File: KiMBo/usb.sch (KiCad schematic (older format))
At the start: 19 parts, among them U1 OSD3358, U6 TPS2051B, U7 TPD4S012, U8 74LVC2G241, U9 TPD4S012

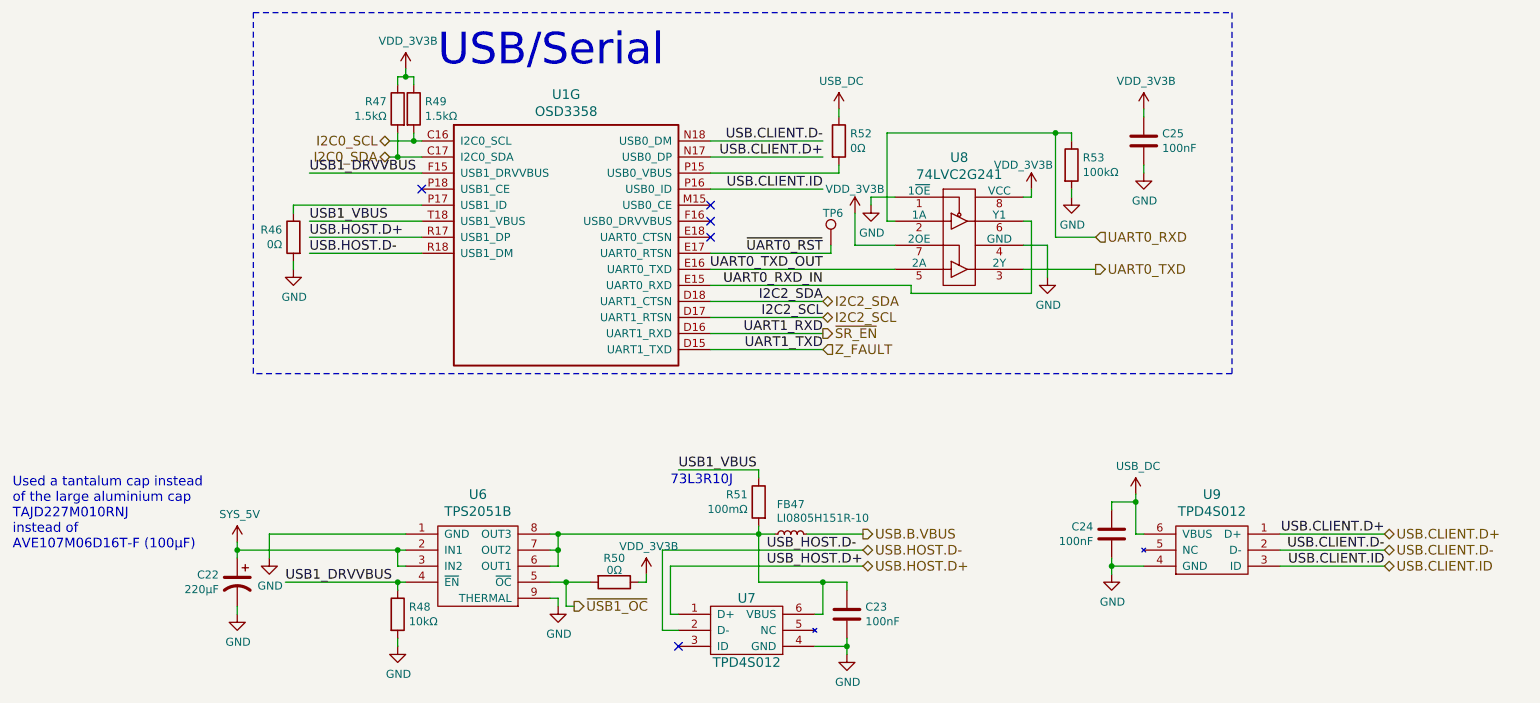
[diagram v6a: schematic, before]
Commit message: Remove the unneeded oscillator, track down which components are underneath the OSD3358 and put them on the top
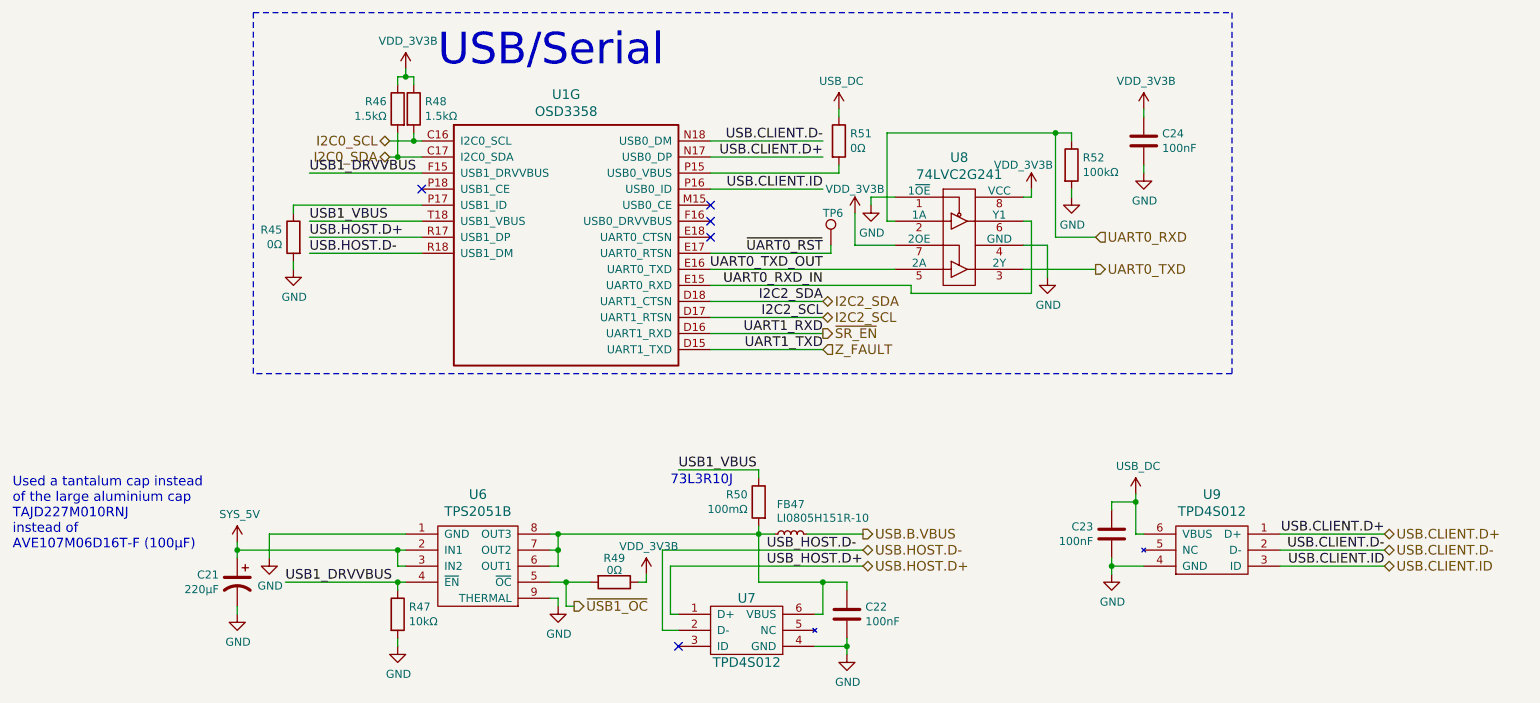
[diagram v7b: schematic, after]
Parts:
- renumbered C22 to C21, C23 to C22, C24 to C23, C25 to C24, R46 to R45, R47 to R46, R48 to R47, R49 to R48, R50 to R49, R51 to R50, R52 to R51, R53 to R52
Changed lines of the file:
@@
 $EndComp
 $Comp
-L GND #PWR099
+L GND #PWR097
 U 1 1 584F5078
 P 7550 2500
-F 0 "#PWR099" H 7550 2250 50  0001 C CNN
+F 0 "#PWR097" H 7550 2250 50  0001 C CNN
 F 1 "GND" H 7555 2327 50  0000 C CNN
 F 2 "" H 7550 2500 50  0000 C CNN
@@
 UART0_RXD_IN
 $Comp
-L R R53
+L R R52
 U 1 1 584F5085
 P 7700 1800
-F 0 "R53" H 7770 1846 50  0000 L CNN
+F 0 "R52" H 7770 1846 50  0000 L CNN
 F 1 "100kΩ" H 7770 1755 50  0000 L CNN
 F 2 "Resistors_SMD:R_0603" V 7630 1800 50  0001 C CNN
@@
 $EndComp
 $Comp
-L GND #PWR0100
+L GND #PWR098
 U 1 1 584F508C
 P 6450 2050
-F 0 "#PWR0100" H 6450 1800 50  0001 C CNN
+F 0 "#PWR098" H 6450 1800 50  0001 C CNN
 F 1 "GND" H 6455 1877 50  0000 C CNN
 F 2 "" H 6450 2050 50  0000 C CNN
@@
 UART0_TXD_OUT
 $Comp
-L GND #PWR0101
+L GND #PWR099
 U 1 1 584F509A
 P 7700 2000
-F 0 "#PWR0101" H 7700 1750 50  0001 C CNN
+F 0 "#PWR099" H 7700 1750 50  0001 C CNN
 F 1 "GND" H 7705 1827 50  0000 C CNN
 F 2 "" H 7700 2000 50  0000 C CNN
@@
 $EndComp
 $Comp
-L C C25
+L C C24
 U 1 1 584F50A3
 P 8150 1650
-F 0 "C25" H 8265 1696 50  0000 L CNN
+F 0 "C24" H 8265 1696 50  0000 L CNN
 F 1 "100nF" H 8265 1605 50  0000 L CNN
 F 2 "Capacitors_SMD:C_0603" H 8150 1650 50  0001 C CNN
@@
 $EndComp
 $Comp
-L GND #PWR0102
+L GND #PWR0100
 U 1 1 584F50AA
 P 8150 1850
-F 0 "#PWR0102" H 8150 1600 50  0001 C CNN
+F 0 "#PWR0100" H 8150 1600 50  0001 C CNN
 F 1 "GND" H 8155 1677 50  0000 C CNN
 F 2 "" H 8150 1850 50  0000 C CNN
@@
 NoConn ~ 5450 2150
 $Comp
-L R R52
+L R R51
 U 1 1 584F50C1
 P 6250 1650
-F 0 "R52" H 6320 1696 50  0000 L CNN
+F 0 "R51" H 6320 1696 50  0000 L CNN
 F 1 "0Ω" H 6320 1605 50  0000 L CNN
 F 2 "Resistors_SMD:R_0603" V 6180 1650 50  0001 C CNN
@@
 NoConn ~ 3650 1950
 $Comp
-L R R46
+L R R45
 U 1 1 584F50D1
 P 2850 2250
-F 0 "R46" H 2920 2296 50  0000 L CNN
+F 0 "R45" H 2920 2296 50  0000 L CNN
 F 1 "0Ω" H 2920 2205 50  0000 L CNN
 F 2 "Resistors_SMD:R_0603" V 2780 2250 50  0001 C CNN
@@
 $EndComp
 $Comp
-L GND #PWR0103
+L GND #PWR0101
 U 1 1 584F50D8
 P 2850 2450
-F 0 "#PWR0103" H 2850 2200 50  0001 C CNN
+F 0 "#PWR0101" H 2850 2200 50  0001 C CNN
 F 1 "GND" H 2855 2277 50  0000 C CNN
 F 2 "" H 2850 2450 50  0000 C CNN
@@
 USB1_DRVVBUS
 $Comp
-L R R47
+L R R46
 U 1 1 584F50E0
 P 3500 1450
-F 0 "R47" H 3569 1496 50  0000 L CNN
+F 0 "R46" H 3569 1496 50  0000 L CNN
 F 1 "1.5kΩ" H 3569 1405 50  0000 L CNN
 F 2 "Resistors_SMD:R_0603" V 3430 1450 50  0001 C CNN
@@
 $EndComp
 $Comp
-L R R49
+L R R48
 U 1 1 584F50E7
 P 3600 1450
-F 0 "R49" H 3670 1496 50  0000 L CNN
+F 0 "R48" H 3670 1496 50  0000 L CNN
 F 1 "1.5kΩ" H 3670 1405 50  0000 L CNN
 F 2 "Resistors_SMD:R_0603" V 3530 1450 50  0001 C CNN
@@
 $EndComp
 $Comp
-L C C23
+L C C22
 U 1 1 58524285
 P 6300 4600
-F 0 "C23" H 6415 4646 50  0000 L CNN
+F 0 "C22" H 6415 4646 50  0000 L CNN
 F 1 "100nF" H 6415 4555 50  0000 L CNN
 F 2 "Capacitors_SMD:C_0603" H 6300 4600 50  0001 C CNN
@@
 $EndComp
 $Comp
-L GND #PWR0104
+L GND #PWR0102
 U 1 1 585243B8
 P 6300 4850
-F 0 "#PWR0104" H 6300 4600 50  0001 C CNN
+F 0 "#PWR0102" H 6300 4600 50  0001 C CNN
 F 1 "GND" H 6305 4677 50  0000 C CNN
 F 2 "" H 6300 4850 50  0000 C CNN
@@
 $EndComp
 $Comp
-L GND #PWR0105
+L GND #PWR0103
 U 1 1 58528602
 P 4500 4550
-F 0 "#PWR0105" H 4500 4300 50  0001 C CNN
+F 0 "#PWR0103" H 4500 4300 50  0001 C CNN
 F 1 "GND" H 4505 4377 50  0000 C CNN
 F 2 "" H 4500 4550 50  0000 C CNN
@@
 $EndComp
 $Comp
-L R R50
+L R R49
 U 1 1 58528C30
 P 4850 4400
-F 0 "R50" V 4700 4400 50  0000 C CNN
+F 0 "R49" V 4700 4400 50  0000 C CNN
 F 1 "0Ω" V 4775 4400 50  0000 C CNN
 F 2 "Resistors_SMD:R_0603" V 4780 4400 50  0001 C CNN
@@
 $EndComp
 $Comp
-L GND #PWR0106
+L GND #PWR0104
 U 1 1 5852A6BE
 P 2500 4600
-F 0 "#PWR0106" H 2500 4350 50  0001 C CNN
+F 0 "#PWR0104" H 2500 4350 50  0001 C CNN
 F 1 "GND" H 2505 4427 50  0000 C CNN
 F 2 "" H 2500 4600 50  0000 C CNN
@@
 $EndComp
 $Comp
-L GND #PWR0107
+L GND #PWR0105
 U 1 1 5852A82F
 P 2700 4250
-F 0 "#PWR0107" H 2700 4000 50  0001 C CNN
+F 0 "#PWR0105" H 2700 4000 50  0001 C CNN
 F 1 "GND" H 2705 4077 50  0000 C CNN
 F 2 "" H 2700 4250 50  0000 C CNN
@@
 USB1_DRVVBUS
 $Comp
-L R R48
+L R R47
 U 1 1 5852B51B
 P 3500 4600
-F 0 "R48" H 3570 4646 50  0000 L CNN
+F 0 "R47" H 3570 4646 50  0000 L CNN
 F 1 "10kΩ" H 3570 4555 50  0000 L CNN
 F 2 "Resistors_SMD:R_0603" V 3430 4600 50  0001 C CNN
@@
 $EndComp
 $Comp
-L GND #PWR0108
+L GND #PWR0106
 U 1 1 5852B68C
 P 3500 4800
-F 0 "#PWR0108" H 3500 4550 50  0001 C CNN
+F 0 "#PWR0106" H 3500 4550 50  0001 C CNN
 F 1 "GND" H 3505 4627 50  0000 C CNN
 F 2 "" H 3500 4800 50  0000 C CNN
@@
 $EndComp
 $Comp
-L C C24
+L C C23
 U 1 1 5852C2E6
 P 7950 4100
-F 0 "C24" H 8065 4146 50  0000 L CNN
+F 0 "C23" H 8065 4146 50  0000 L CNN
 F 1 "100nF" H 8065 4055 50  0000 L CNN
 F 2 "Capacitors_SMD:C_0603" H 7950 4100 50  0001 C CNN
@@
 I2C2_SDA
 $Comp
-L USB_DC #PWR0109
+L USB_DC #PWR0107
 U 1 1 59F94F9A
 P 8100 3850
-F 0 "#PWR0109" H 8100 3700 50  0001 C CNN
+F 0 "#PWR0107" H 8100 3700 50  0001 C CNN
 F 1 "USB_DC" H 8115 4023 50  0000 C CNN
 F 2 "" H 8100 3850 50  0000 C CNN
@@
 $EndComp
 $Comp
-L SYS_5V #PWR0110
+L SYS_5V #PWR0108
 U 1 1 59F970D0
 P 2500 4150
-F 0 "#PWR0110" H 2500 4000 50  0001 C CNN
+F 0 "#PWR0108" H 2500 4000 50  0001 C CNN
 F 1 "SYS_5V" H 2515 4323 50  0000 C CNN
 F 2 "" H 2500 4150 50  0000 C CNN
@@
 $EndComp
 $Comp
-L VDD_3V3B #PWR0111
+L VDD_3V3B #PWR0109
 U 1 1 59FBF8B1
 P 6350 2100
-F 0 "#PWR0111" H 6350 1950 50  0001 C CNN
+F 0 "#PWR0109" H 6350 1950 50  0001 C CNN
 F 1 "VDD_3V3B" H 6350 2250 50  0000 C CNN
 F 2 "" H 6350 2100 50  0000 C CNN
@@
 $EndComp
 $Comp
-L VDD_3V3B #PWR0112
+L VDD_3V3B #PWR0110
 U 1 1 59FBF8FC
 P 7450 1950
-F 0 "#PWR0112" H 7450 1800 50  0001 C CNN
+F 0 "#PWR0110" H 7450 1800 50  0001 C CNN
 F 1 "VDD_3V3B" H 7400 2100 50  0000 C CNN
 F 2 "" H 7450 1950 50  0000 C CNN
@@
 $EndComp
 $Comp
-L VDD_3V3B #PWR0113
+L VDD_3V3B #PWR0111
 U 1 1 59FC0162
 P 8150 1450
-F 0 "#PWR0113" H 8150 1300 50  0001 C CNN
+F 0 "#PWR0111" H 8150 1300 50  0001 C CNN
 F 1 "VDD_3V3B" H 8165 1623 50  0000 C CNN
 F 2 "" H 8150 1450 50  0000 C CNN
@@
 $EndComp
 $Comp
-L USB_DC #PWR0114
+L USB_DC #PWR0112
 U 1 1 59FEDDB0
 P 6250 1450
-F 0 "#PWR0114" H 6250 1300 50  0001 C CNN
+F 0 "#PWR0112" H 6250 1300 50  0001 C CNN
 F 1 "USB_DC" H 6265 1623 50  0000 C CNN
 F 2 "" H 6250 1450 50  0000 C CNN
@@
 $EndComp
 $Comp
-L VDD_3V3B #PWR0115
+L VDD_3V3B #PWR0113
 U 1 1 5A01DA26
 P 3550 1200
-F 0 "#PWR0115" H 3550 1050 50  0001 C CNN
+F 0 "#PWR0113" H 3550 1050 50  0001 C CNN
 F 1 "VDD_3V3B" H 3565 1373 50  0000 C CNN
 F 2 "" H 3550 1200 50  0000 C CNN
@@
 Used a tantalum cap instead\nof the large aluminium cap\nTAJD227M010RNJ\ninstead of\nAVE107M06D16T-F (100μF)
 $Comp
-L VDD_3V3B #PWR0116
+L VDD_3V3B #PWR0114
 U 1 1 5AF563FC
 P 5050 4350
-F 0 "#PWR0116" H 5050 4200 50  0001 C CNN
+F 0 "#PWR0114" H 5050 4200 50  0001 C CNN
 F 1 "VDD_3V3B" H 5065 4523 50  0000 C CNN
 F 2 "" H 5050 4350 50  0000 C CNN
@@
 $EndComp
 $Comp
-L GND #PWR0117
+L GND #PWR0115
 U 1 1 5BC77EEA
 P 7950 4350
-F 0 "#PWR0117" H 7950 4100 50  0001 C CNN
+F 0 "#PWR0115" H 7950 4100 50  0001 C CNN
 F 1 "GND" H 7955 4177 50  0000 C CNN
 F 2 "" H 7950 4350 50  0000 C CNN
@@
 	6200 2350 6200 2300
 $Comp
-L R R51
+L R R50
 U 1 1 58DC7D9A
 P 5750 3900
-F 0 "R51" H 5819 3946 50  0000 L CNN
+F 0 "R50" H 5819 3946 50  0000 L CNN
 F 1 "100mΩ" H 5819 3855 50  0000 L CNN
 F 2 "Resistors_SMD:R_0603" V 5680 3900 50  0001 C CNN
@@
 73L3R10J
 $Comp
-L CP1 C22
+L CP1 C21
 U 1 1 58EB0DF2
 P 2500 4400
-F 0 "C22" H 2615 4446 50  0000 L CNN
+F 0 "C21" H 2615 4446 50  0000 L CNN
 F 1 "220μF" H 2615 4355 50  0000 L CNN
 F 2 "Capacitors_Tantalum_SMD:TantalC_SizeD_EIA-7343_Reflow" H 2500 4400 50  0001 C CNN
